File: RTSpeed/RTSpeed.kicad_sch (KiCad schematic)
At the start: 1 part, among them U4 STM32F411CEUx

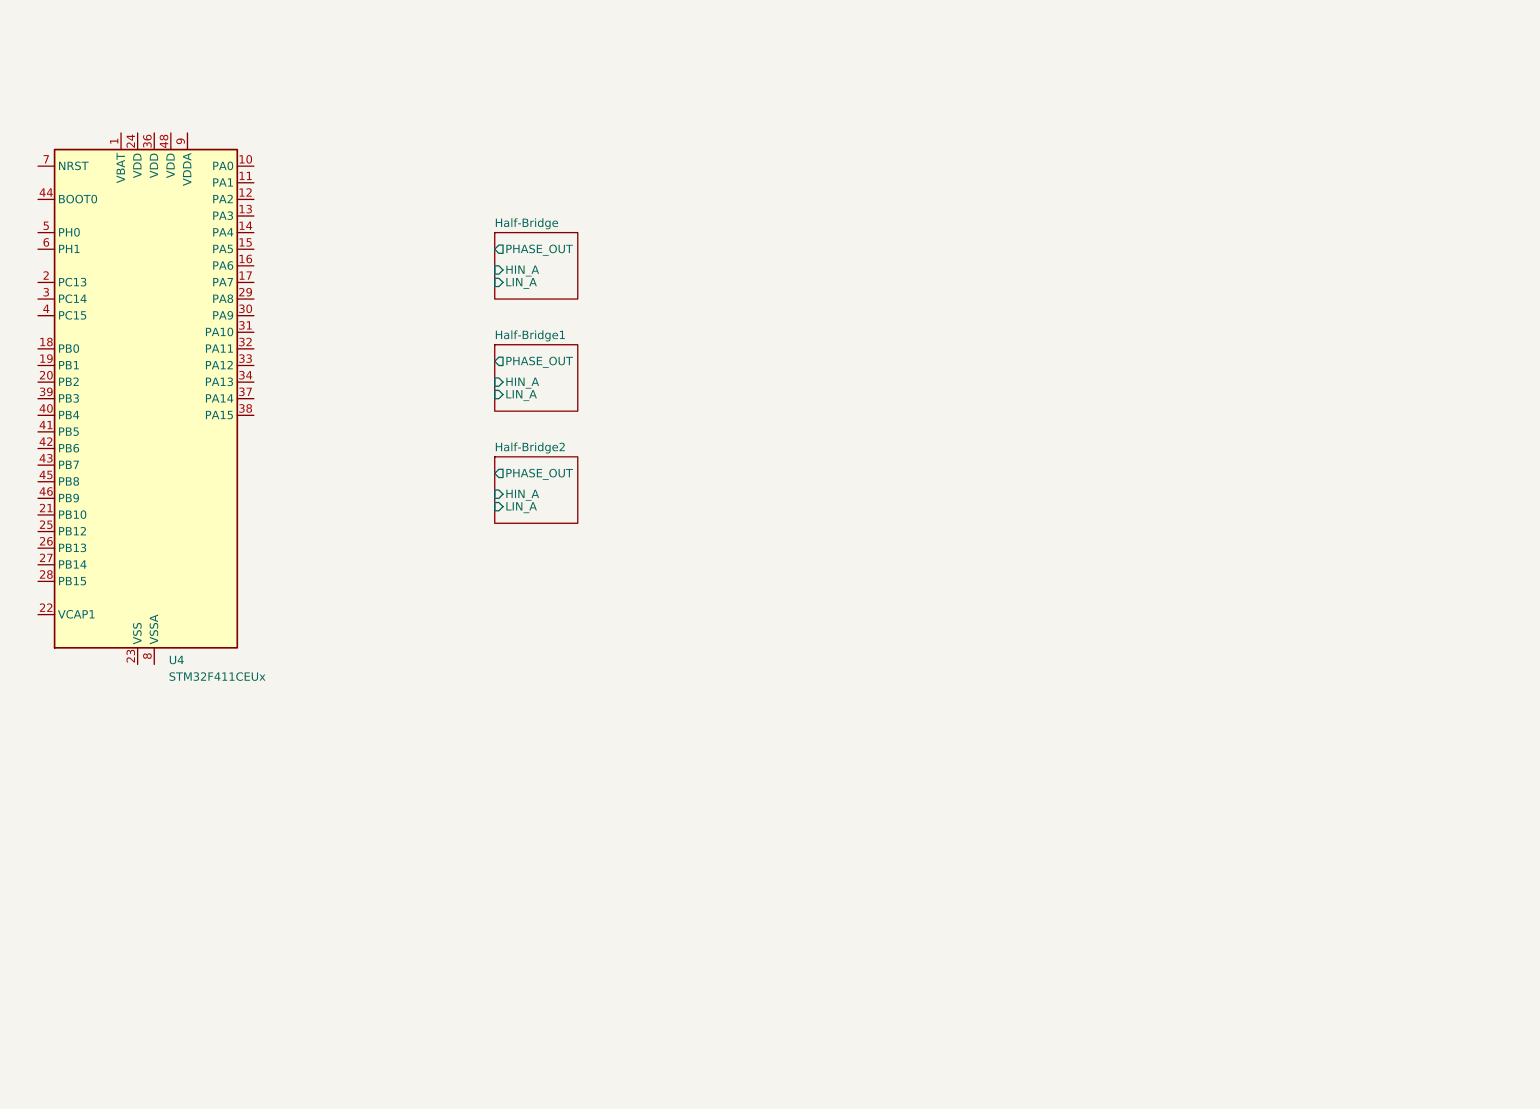
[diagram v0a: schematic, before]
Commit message: Added STM32F411 development schematic
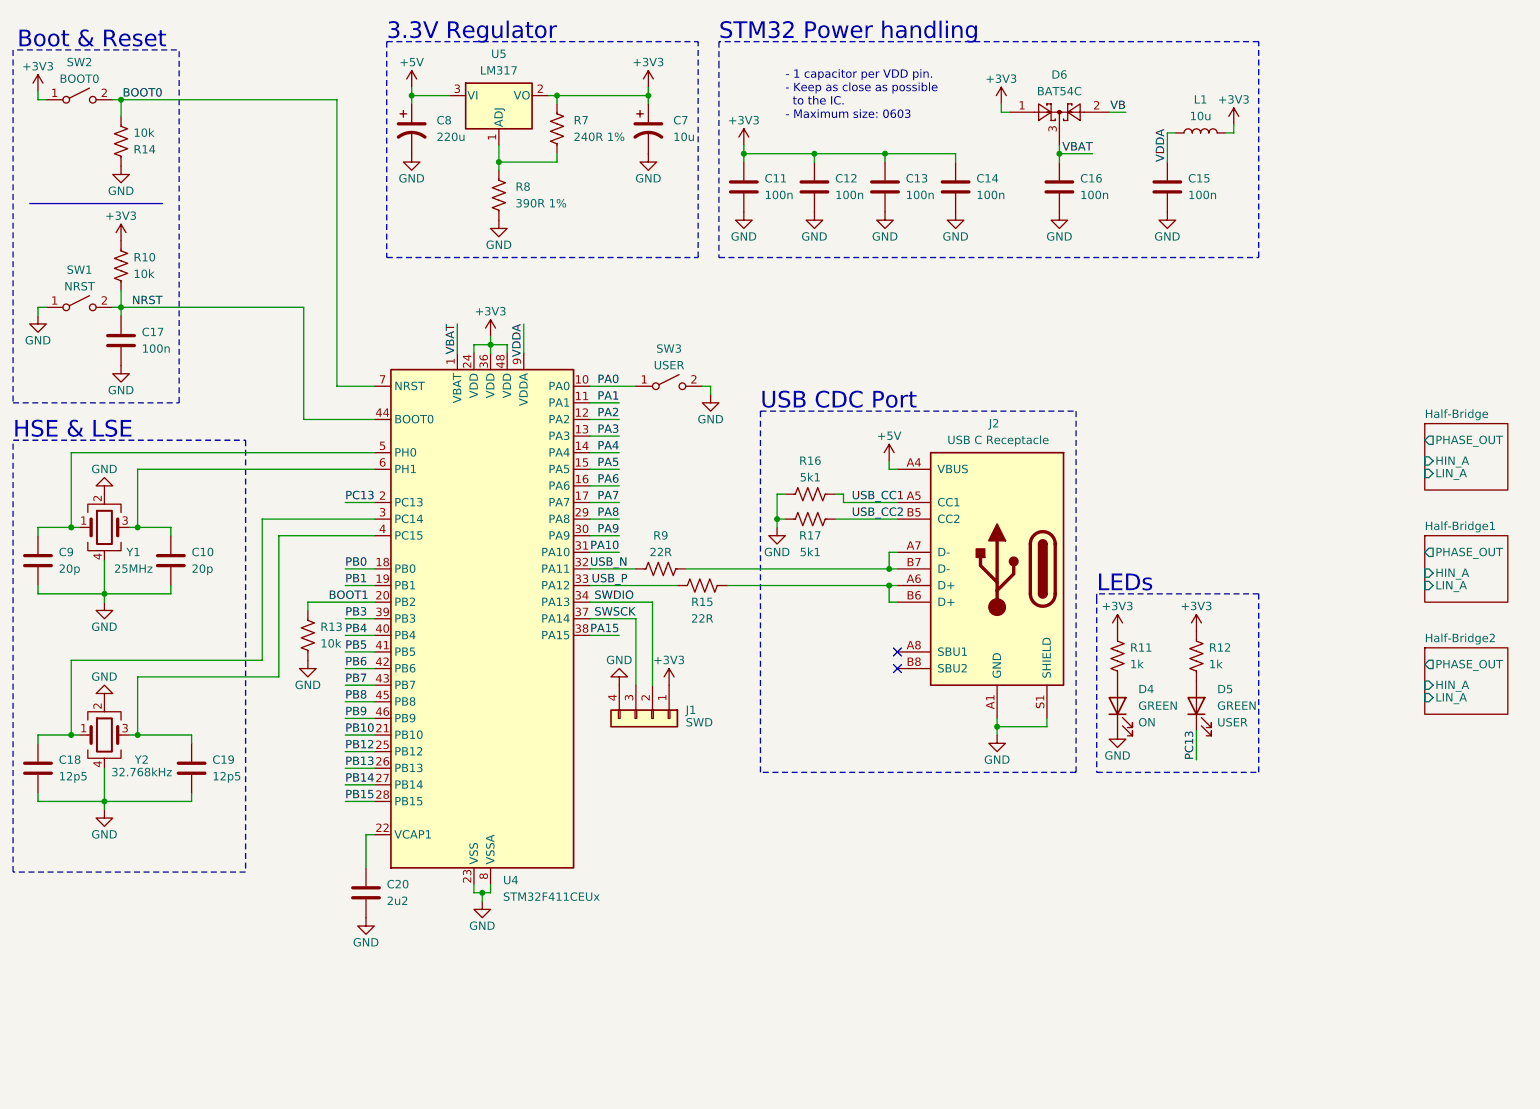
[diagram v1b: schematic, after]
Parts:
- added C10, C9: 20p, symbol Device:C
- added C11, C12, C13, C14, C15, C16, C17: 100n, symbol Device:C
- added C18, C19: 12p5, symbol Device:C
- added C20: 2u2, symbol Device:C
- added C7: 10u, symbol Device:C_Polarized_US
- added C8: 220u, symbol Device:C_Polarized_US
- added D4, D5: GREEN, symbol Device:LED
- added D6: BAT54C, Package_TO_SOT_SMD:SOT-23, symbol Diode:BAT54C
- added J1: SWD, symbol Connector_Generic:Conn_01x04
- added J2: USB C Receptacle, symbol Connector:USB_C_Receptacle_USB2.0_16P
- added L1: 10u, symbol Device:L
- added R10, R13, R14: 10k, symbol Device:R_US
- added R11, R12: 1k, symbol Device:R_US
- added R15, R9: 22R, symbol Device:R_US
- added R16, R17: 5k1, symbol Device:R_US
- added R7: 240R 1%, symbol Device:R_US
- added R8: 390R 1%, symbol Device:R_US
- added SW1: NRST, symbol Switch:SW_SPST
- added SW2: BOOT0, symbol Switch:SW_SPST
- added SW3: USER, symbol Switch:SW_SPST
- added U5: LM317, Package_TO_SOT_THT:TO-220-3_Vertical, symbol Regulator_Linear:LM317_TO-220
- added Y1: 25MHz, symbol Device:Crystal_GND24
- added Y2: 32.768kHz, symbol Device:Crystal_GND24
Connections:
- net VBAT: now reaches U4.1 (VBAT)
- net VBAT: now also C16.1, D6.3
- net PA0: now reaches U4.10 (PA0)
- net PA0: now also SW3.1 (A)
- net PA1: now reaches U4.11 (PA1)
- net PA2: now reaches U4.12 (PA2)
- net PA3: now reaches U4.13 (PA3)
- net PA4: now reaches U4.14 (PA4)
- net PA5: now reaches U4.15 (PA5)
- net PA6: now reaches U4.16 (PA6)
- net PA7: now reaches U4.17 (PA7)
- net PB0: now reaches U4.18 (PB0)
- net PB1: now reaches U4.19 (PB1)
- net PC13: now reaches U4.2 (PC13)
- net PC13: now also D5.1 (K)
- net BOOT1: now reaches U4.20 (PB2)
- net BOOT1: now also R13.1
- net PB10: now reaches U4.21 (PB10)
- net at U4.22 (VCAP1): now also C20.1
- net GND: now reaches U4.23 (VSS), U4.35 (VSS), U4.47 (VSS), U4.49 (VSS)
- net GND: now also U4.8 (VSSA), C10.2, C11.2, C12.2, C13.2, C14.2, C15.2, C16.2, C17.1, C18.2, C19.2, C20.2, C7.2, C8.2, C9.2, D4.1 (K), J1.4 (Pin_4), J2.A1 (GND), J2.A12 (GND), J2.B1 (GND), J2.B12 (GND), J2.S1 (SHIELD), R13.2, R14.1, R16.1, R17.1, R8.2, SW1.1 (A), SW3.2 (B), Y1.2, Y1.4, Y2.2, Y2.4
- net +3V3: now reaches U4.24 (VDD)
- net +3V3: now also U4.36 (VDD), U4.48 (VDD), C11.1, C12.1, C13.1, C14.1, C7.1, D6.1, J1.1 (Pin_1), L1.2, R10.1, R11.1, R12.1, R7.1, SW2.1 (A), U5.2 (VO)
- net PB12: now reaches U4.25 (PB12)
- net PB13: now reaches U4.26 (PB13)
- net PB14: now reaches U4.27 (PB14)
- net PB15: now reaches U4.28 (PB15)
- net PA8: now reaches U4.29 (PA8)
- net at U4.3 (PC14): now also C18.1, Y2.1
- net PA9: now reaches U4.30 (PA9)
- net PA10: now reaches U4.31 (PA10)
- net USB_N: now reaches U4.32 (PA11)
- net USB_N: now also R9.1
- net USB_P: now reaches U4.33 (PA12)
- net USB_P: now also R15.1
- net SWDIO: now reaches U4.34 (PA13)
- net SWDIO: now also J1.2 (Pin_2)
- net SWSCK: now reaches U4.37 (PA14)
- net SWSCK: now also J1.3 (Pin_3)
- net PA15: now reaches U4.38 (PA15)
- net PB3: now reaches U4.39 (PB3)
- net at U4.4 (PC15): now also C19.1, Y2.3
- net PB4: now reaches U4.40 (PB4)
- net PB5: now reaches U4.41 (PB5)
- net PB6: now reaches U4.42 (PB6)
- net PB7: now reaches U4.43 (PB7)
- net NRST: now reaches U4.44 (BOOT0)
- net NRST: now also C17.2, R10.2, SW1.2 (B)
- net PB8: now reaches U4.45 (PB8)
- net PB9: now reaches U4.46 (PB9)
- net at U4.5 (PH0): now also C9.1, Y1.1
- net at U4.6 (PH1): now also C10.1, Y1.3
- net BOOT0: now reaches U4.7 (NRST)
- net BOOT0: now also R14.2, SW2.2 (B)
- net VDDA: now reaches U4.9 (VDDA)
- net VDDA: now also C15.1, L1.1
- new net: R7.2, R8.1, U5.1 (ADJ)
- new net: D5.2 (A), R12.2
- new net: J2.A6 (D+), J2.B6 (D+), R15.2
- new net: D4.2 (A), R11.2
- new net: J2.A7 (D-), J2.B7 (D-), R9.2
- new net +5V: C8.1, J2.A4 (VBUS), J2.A9 (VBUS), J2.B4 (VBUS), J2.B9 (VBUS), U5.3 (VI)
- new net USB_CC1: J2.A5 (CC1), R16.2
- new net USB_CC2: J2.B5 (CC2), R17.2
- new net VB: D6.2
- no-connect marks 0 -> 2
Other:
- note added: "- 1 capacitor per VDD pin. - Keep as close as possible to the IC. - Maximum size: 0603"
- note added: "3.3V Regulator"
- note added: "Boot & Reset"
- note added: "HSE & LSE"
- note added: "LEDs"
- note added: "STM32 Power handling"
- note added: "USB CDC Port"
- moved on the sheet: U4

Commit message: Connected Inverter
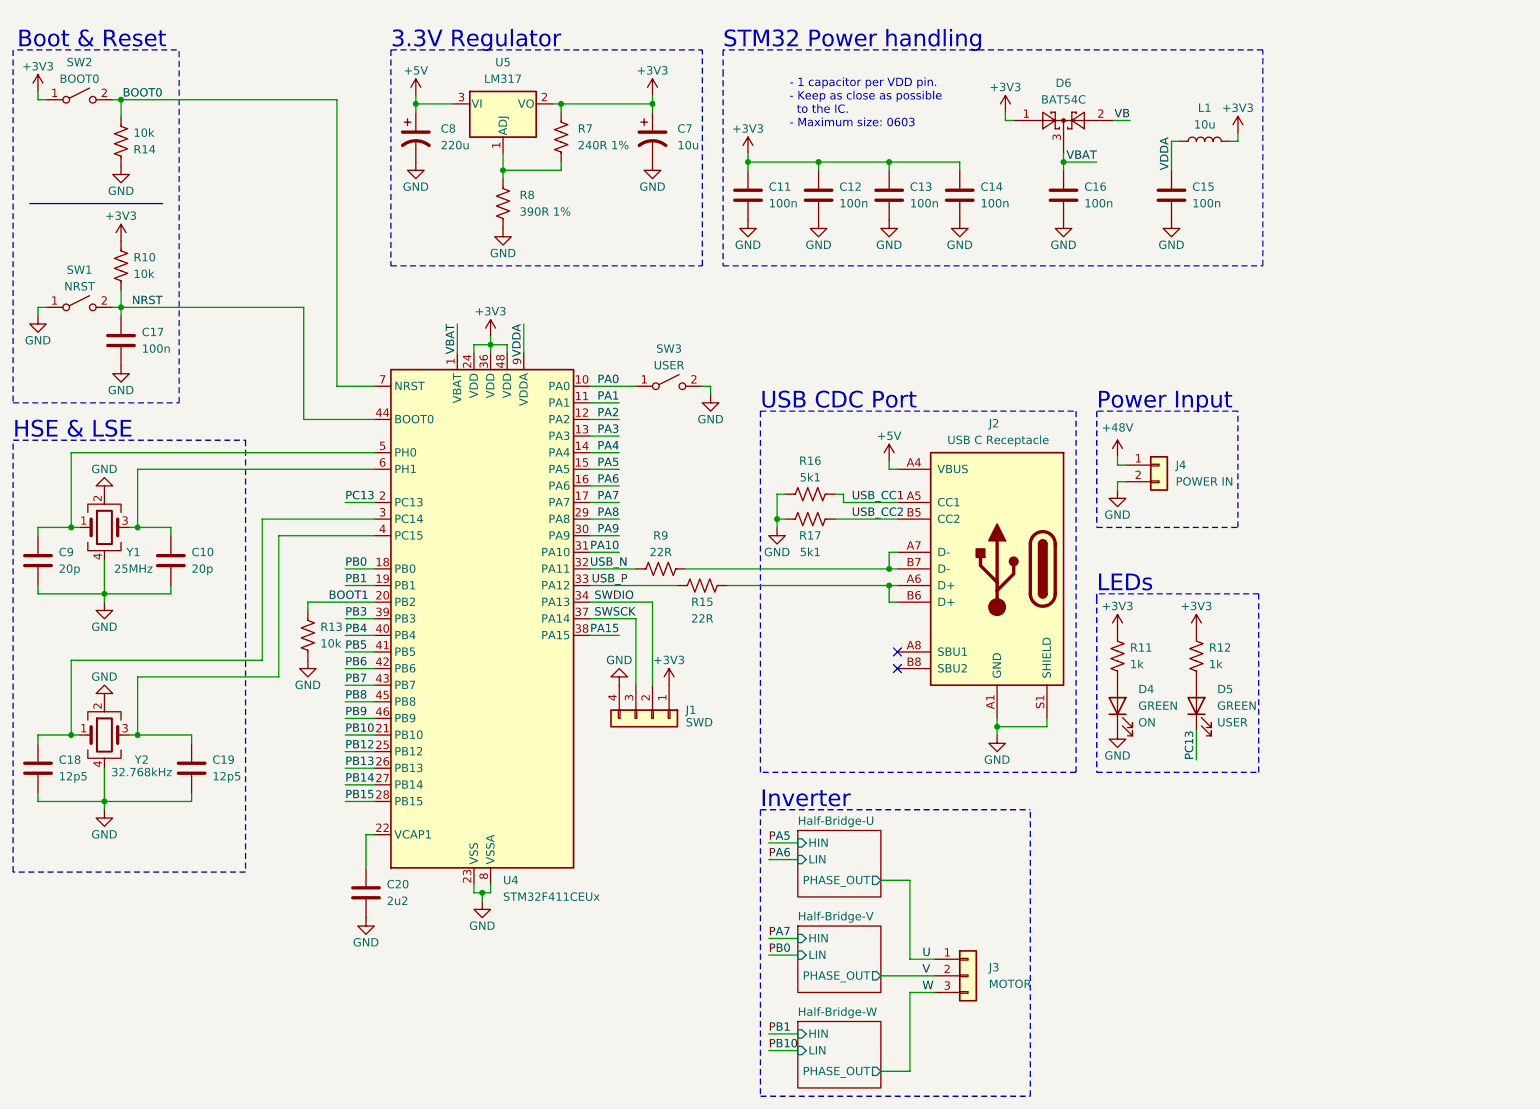
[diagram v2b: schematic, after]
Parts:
- added J3: MOTOR, symbol Connector_Generic:Conn_01x03
- added J4: POWER IN, symbol Connector_Generic:Conn_01x02
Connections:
- net GND: now also J4.2 (Pin_2)
- new net +48V: J4.1 (Pin_1)
- new net U: J3.1 (Pin_1)
- new net V: J3.2 (Pin_2)
- new net W: J3.3 (Pin_3)
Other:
- sheet Half-Bridge renamed Half-Bridge-U
- removed sheet Half-Bridge1
- removed sheet Half-Bridge2
- added sheet Half-Bridge-V (Half-Bridge.kicad_sch)
- added sheet Half-Bridge-W (Half-Bridge.kicad_sch)
- sheet Half-Bridge-U ports: added HIN, LIN; removed HIN_A, LIN_A
- note added: "Inverter"
- note added: "Power Input"
- title: (none) -> RTSpeed
- moved on the sheet: C11, C12, C13, C14, C15, C16, C7, C8, D6, L1, R7, R8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
